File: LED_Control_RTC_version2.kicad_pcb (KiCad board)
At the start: 4 copper layers, 100 x 80 mm, 142 parts, among them J1 Screw_Terminal_01x02, J10 Conn_01x06_Male, J2 Conn_01x02, J3 Conn_02x04_Odd_Even, J4 DS1023-2*8SF11, J5 DS1023-2*8SF11, J6 Conn_01x03_Female, J7 Conn_ARM_JTAG_SWD_10, J8 Conn_ARM_JTAG_SWD_10, J9 Conn_01x06_Male, Q1 IRLR8726TRPBF, Q10 IRLR8726TRPBF, Q11 PJM2309PSA, Q2 IRLR8726TRPBF, Q3 IRLR8726TRPBF, Q4 IRLR8726TRPBF, Q5 IRLR8726TRPBF, Q6 IRLR8726TRPBF, Q7 IRLR8726TRPBF, Q8 IRLR8726TRPBF, Q9 IRLR8726TRPBF, U1 STM32F103C8Tx, U101 TC4427, U102 TC4427, U103 TC4427, U104 TC4427, U105 TC4427, U2 STM32G030C6Tx, U3 AT24C16D-XHM-B, U4 MAX3485, U5 TPS5401, U6 LM1117-3.3, Y1 16MHz, Y2 32.768KHz

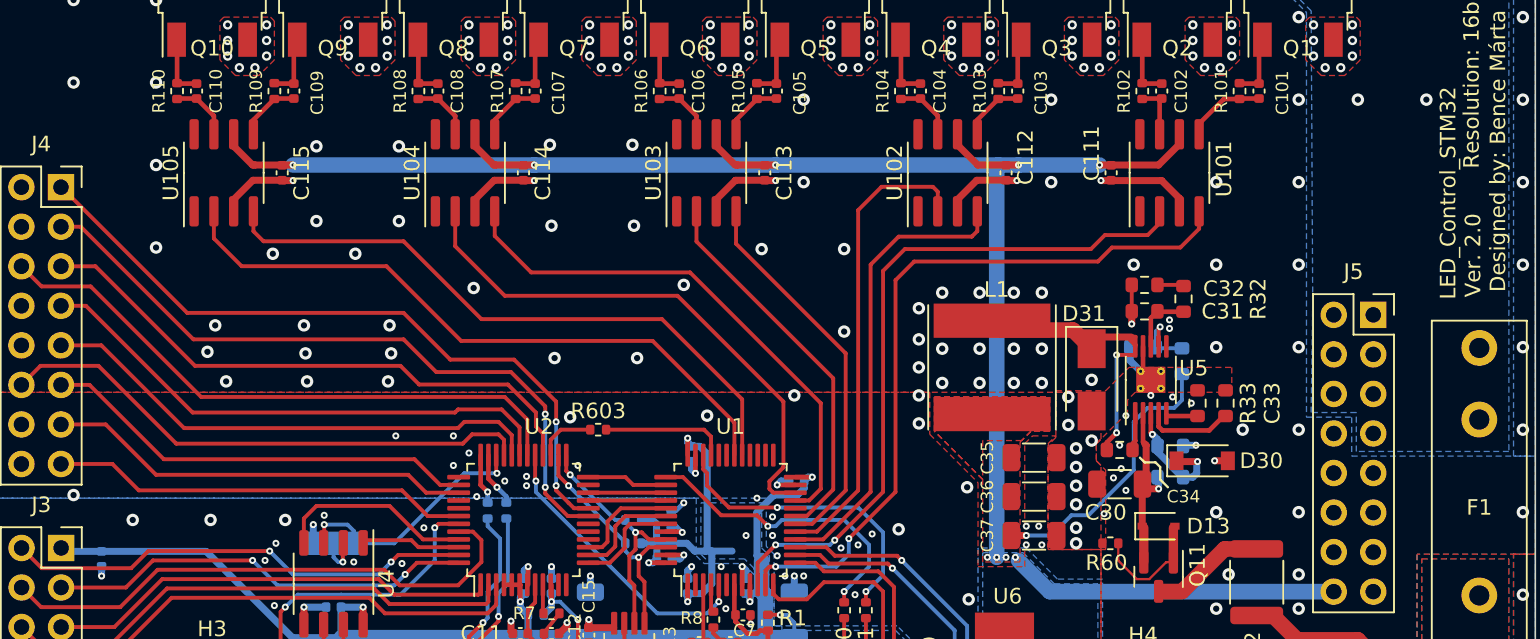
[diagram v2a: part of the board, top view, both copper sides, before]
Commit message: Added more GND vias
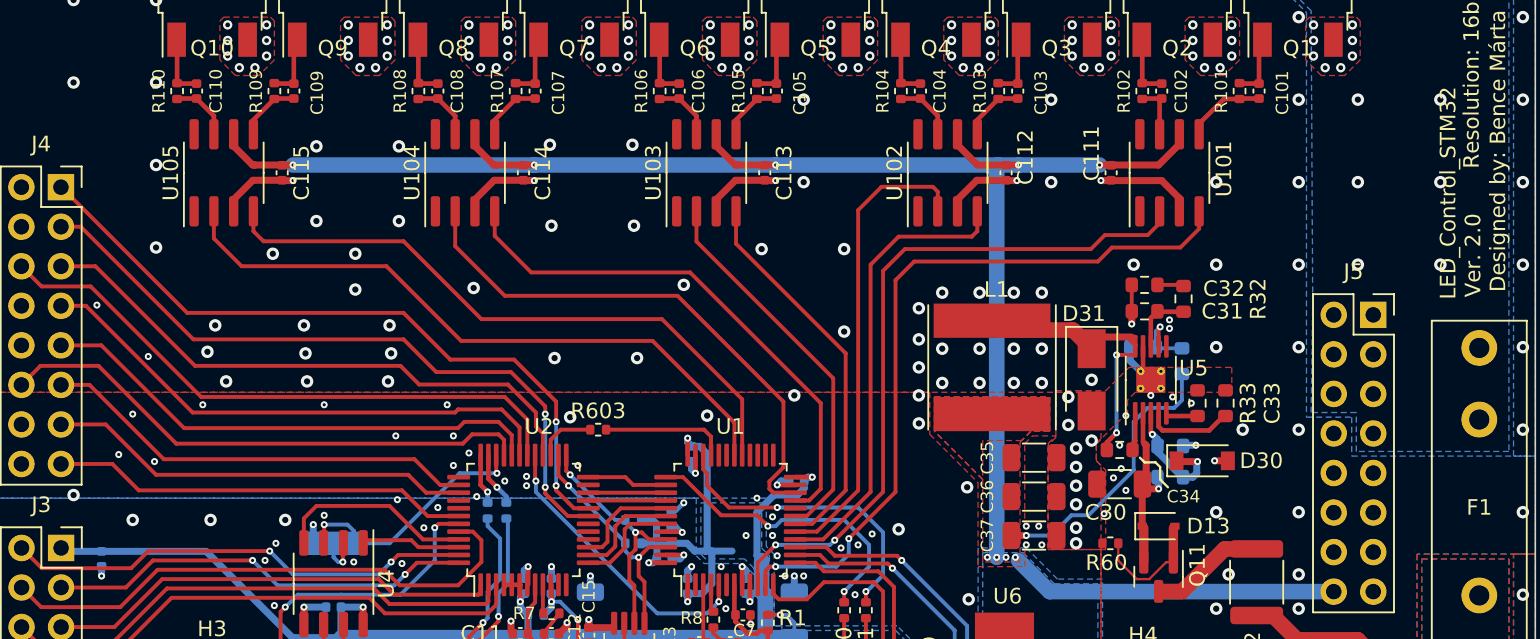
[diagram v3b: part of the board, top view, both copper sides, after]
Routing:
- net GND: vias 369 -> 384
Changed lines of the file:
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@@
   (via (at 165.25 79.5) (size 0.6) (drill 0.3) (layers "F.Cu" "B.Cu") (net 2))
   (via (at 140.3 111.55) (size 0.45) (drill 0.2) (layers "F.Cu" "B.Cu") (free) (net 2))
+  (via (at 125.1 101.9) (size 0.45) (drill 0.2) (layers "F.Cu" "B.Cu") (net 2))
   (via (at 163.3 98.3) (size 0.8) (drill 0.4) (layers "F.Cu" "B.Cu") (free) (net 2))
   (via (at 174.5 92.9) (size 0.8) (drill 0.4) (layers "F.Cu" "B.Cu") (free) (net 2))
@@
   (via (at 159.3 98.3) (size 0.8) (drill 0.4) (layers "F.Cu" "B.Cu") (free) (net 2))
   (via (at 159.25 80.25) (size 0.6) (drill 0.3) (layers "F.Cu" "B.Cu") (net 2))
+  (via (at 188.9 92.9) (size 0.8) (drill 0.4) (layers "F.Cu" "B.Cu") (free) (net 2))
   (via (at 101.1 81.2) (size 0.8) (drill 0.4) (layers "F.Cu" "B.Cu") (free) (net 2))
   (via (at 109.9 109.3) (size 0.8) (drill 0.4) (layers "F.Cu" "B.Cu") (free) (net 2))
@@
   (via (at 127 107.8) (size 0.45) (drill 0.2) (layers "F.Cu" "B.Cu") (net 2))
   (via (at 182.3 119.5) (size 0.8) (drill 0.4) (layers "F.Cu" "B.Cu") (free) (net 2))
+  (via (at 183.6 82.3) (size 0.8) (drill 0.4) (layers "F.Cu" "B.Cu") (free) (net 2))
   (via (at 151.3 114.1) (size 0.45) (drill 0.2) (layers "F.Cu" "B.Cu") (free) (net 2))
   (via (at 129 78.5) (size 0.6) (drill 0.3) (layers "F.Cu" "B.Cu") (net 2))
@@
   (via (at 115.9 96.8) (size 0.8) (drill 0.4) (layers "F.Cu" "B.Cu") (free) (net 2))
   (via (at 95.8 123.6) (size 0.8) (drill 0.4) (layers "F.Cu" "B.Cu") (free) (net 2))
+  (via (at 105.9 98.8) (size 0.45) (drill 0.2) (layers "F.Cu" "B.Cu") (net 2))
   (via (at 119.2 92.2) (size 0.8) (drill 0.4) (layers "F.Cu" "B.Cu") (free) (net 2))
   (via (at 129 79.5) (size 0.6) (drill 0.3) (layers "F.Cu" "B.Cu") (net 2))
@@
   (via (at 142 77.5) (size 0.6) (drill 0.3) (layers "F.Cu" "B.Cu") (net 2))
   (via (at 155.4 99.5) (size 0.8) (drill 0.4) (layers "F.Cu" "B.Cu") (free) (net 2))
+  (via (at 188.9 82.3) (size 0.8) (drill 0.4) (layers "F.Cu" "B.Cu") (free) (net 2))
   (via (at 194.2 103.5) (size 0.8) (drill 0.4) (layers "F.Cu" "B.Cu") (free) (net 2))
   (via (at 135 80.25) (size 0.6) (drill 0.3) (layers "F.Cu" "B.Cu") (net 2))
@@
   (via (at 145.3 91.9) (size 0.8) (drill 0.4) (layers "F.Cu" "B.Cu") (free) (net 2))
   (via (at 161.4 126) (size 0.45) (drill 0.2) (layers "F.Cu" "B.Cu") (free) (net 2))
+  (via (at 119.2 94.5) (size 0.8) (drill 0.4) (layers "F.Cu" "B.Cu") (free) (net 2))
   (via (at 116.5 109.6) (size 0.45) (drill 0.2) (layers "F.Cu" "B.Cu") (net 2))
+  (via (at 188.9 87.6) (size 0.8) (drill 0.4) (layers "F.Cu" "B.Cu") (free) (net 2))
   (via (at 181.5 80.25) (size 0.6) (drill 0.3) (layers "F.Cu" "B.Cu") (net 2))
   (via (at 175.5 77.5) (size 0.6) (drill 0.3) (layers "F.Cu" "B.Cu") (net 2))
@@
   (via (at 111 79.5) (size 0.6) (drill 0.3) (layers "F.Cu" "B.Cu") (net 2))
   (via (at 165.25 77.5) (size 0.6) (drill 0.3) (layers "F.Cu" "B.Cu") (net 2))
+  (via (at 117.2 101.9) (size 0.45) (drill 0.2) (layers "F.Cu" "B.Cu") (net 2))
   (via (at 174.5 87.6) (size 0.8) (drill 0.4) (layers "F.Cu" "B.Cu") (free) (net 2))
   (via (at 144.5 77.5) (size 0.6) (drill 0.3) (layers "F.Cu" "B.Cu") (net 2))
@@
   (via (at 136.75 79.5) (size 0.6) (drill 0.3) (layers "F.Cu" "B.Cu") (net 2))
   (via (at 136 80.25) (size 0.6) (drill 0.3) (layers "F.Cu" "B.Cu") (net 2))
+  (via (at 104.9 102.5) (size 0.45) (drill 0.2) (layers "F.Cu" "B.Cu") (net 2))
   (via (at 121.4 96.8) (size 0.8) (drill 0.4) (layers "F.Cu" "B.Cu") (free) (net 2))
   (via (at 130.2 107.1) (size 0.45) (drill 0.2) (layers "F.Cu" "B.Cu") (free) (net 2))
@@
   (via (at 117 55.8) (size 0.8) (drill 0.4) (layers "F.Cu" "B.Cu") (free) (net 2))
   (via (at 133 120.4) (size 0.45) (drill 0.2) (layers "F.Cu" "B.Cu") (free) (net 2))
+  (via (at 183.6 87.6) (size 0.8) (drill 0.4) (layers "F.Cu" "B.Cu") (free) (net 2))
   (via (at 121.25 78.5) (size 0.6) (drill 0.3) (layers "F.Cu" "B.Cu") (net 2))
   (via (at 145 107.9) (size 0.45) (drill 0.2) (layers "F.Cu" "B.Cu") (free) (net 2))
@@
   (via (at 169.2 92.9) (size 0.8) (drill 0.4) (layers "F.Cu" "B.Cu") (free) (net 2))
   (via (at 156.9 94.7) (size 0.8) (drill 0.4) (layers "F.Cu" "B.Cu") (free) (net 2))
+  (via (at 102.6 95.5) (size 0.45) (drill 0.2) (layers "F.Cu" "B.Cu") (net 2))
   (via (at 95.8 81.2) (size 0.8) (drill 0.4) (layers "F.Cu" "B.Cu") (free) (net 2))
   (via (at 167.3 108.9) (size 0.45) (drill 0.2) (layers "F.Cu" "B.Cu") (net 2))
@@
   (via (at 138.2 123.6) (size 0.8) (drill 0.4) (layers "F.Cu" "B.Cu") (free) (net 2))
   (via (at 183.6 120.4) (size 0.8) (drill 0.4) (layers "F.Cu" "B.Cu") (free) (net 2))
+  (via (at 106.3 105.55) (size 0.45) (drill 0.2) (layers "F.Cu" "B.Cu") (net 2))
   (via (at 148.8 134.2) (size 0.8) (drill 0.4) (layers "F.Cu" "B.Cu") (free) (net 2))
+  (via (at 104 105.1) (size 0.45) (drill 0.2) (layers "F.Cu" "B.Cu") (net 2))
   (via (at 102.9 112.9) (size 0.45) (drill 0.2) (layers "F.Cu" "B.Cu") (net 2))
   (via (at 113.5 78.5) (size 0.6) (drill 0.3) (layers "F.Cu" "B.Cu") (net 2))
@@
   (via (at 133.5 105.8) (size 0.45) (drill 0.2) (layers "F.Cu" "B.Cu") (free) (net 2))
   (via (at 148 82.3) (size 0.8) (drill 0.4) (layers "F.Cu" "B.Cu") (free) (net 2))
+  (via (at 121.9 108) (size 0.45) (drill 0.2) (layers "F.Cu" "B.Cu") (net 2))
   (via (at 161.5 98.3) (size 0.8) (drill 0.4) (layers "F.Cu" "B.Cu") (free) (net 2))
   (via (at 179.8 115) (size 0.8) (drill 0.4) (layers "F.Cu" "B.Cu") (free) (net 2))
@@
   (via (at 183.6 121.8) (size 0.8) (drill 0.4) (layers "F.Cu" "B.Cu") (free) (net 2))
   (via (at 128.25 80.25) (size 0.6) (drill 0.3) (layers "F.Cu" "B.Cu") (net 2))
+  (via (at 183.6 92.9) (size 0.8) (drill 0.4) (layers "F.Cu" "B.Cu") (free) (net 2))
   (via (at 167.75 79.5) (size 0.6) (drill 0.3) (layers "F.Cu" "B.Cu") (net 2))
   (via (at 138.2 55.8) (size 0.8) (drill 0.4) (layers "F.Cu" "B.Cu") (free) (net 2))
@@
   (via (at 164.7 134.2) (size 0.8) (drill 0.4) (layers "F.Cu" "B.Cu") (free) (net 2))
   (via (at 126.5 78.5) (size 0.6) (drill 0.3) (layers "F.Cu" "B.Cu") (net 2))
+  (via (at 109.4 101.9) (size 0.45) (drill 0.2) (layers "F.Cu" "B.Cu") (net 2))
   (via (at 146.5 55.8) (size 0.8) (drill 0.4) (layers "F.Cu" "B.Cu") (free) (net 2))
   (via (at 116.1 100.4) (size 0.8) (drill 0.4) (layers "F.Cu" "B.Cu") (free) (net 2))
@@
   (via (at 115.2 87.5) (size 0.45) (drill 0.2) (layers "F.Cu" "B.Cu") (net 2))
   (via (at 163.3 94.7) (size 0.8) (drill 0.4) (layers "F.Cu" "B.Cu") (free) (net 2))
-  (via (at 188 82.3) (size 0.8) (drill 0.4) (layers "F.Cu" "B.Cu") (free) (net 2))
   (via (at 163.1 109.7) (size 0.45) (drill 0.2) (layers "F.Cu" "B.Cu") (net 2))
   (via (at 122.197833 112.1) (size 0.45) (drill 0.2) (layers "F.Cu" "B.Cu") (net 2))
@@
   (via (at 121.3 100.4) (size 0.8) (drill 0.4) (layers "F.Cu" "B.Cu") (free) (net 2))
   (via (at 127.25 80.25) (size 0.6) (drill 0.3) (layers "F.Cu" "B.Cu") (net 2))
+  (via (at 124.5 108.5) (size 0.45) (drill 0.2) (layers "F.Cu" "B.Cu") (net 2))
   (via (at 183.25 79.5) (size 0.6) (drill 0.3) (layers "F.Cu" "B.Cu") (net 2))
   (via (at 118.75 77.5) (size 0.6) (drill 0.3) (layers "F.Cu" "B.Cu") (net 2))
@@
   (via (at 194.2 134.2) (size 0.8) (drill 0.4) (layers "F.Cu" "B.Cu") (free) (net 2))
   (via (at 117.8 119.4) (size 0.45) (drill 0.2) (layers "F.Cu" "B.Cu") (net 2))
-  (via (at 183.6 82.3) (size 0.8) (drill 0.4) (layers "F.Cu" "B.Cu") (free) (net 2))
   (via (at 174.5 115) (size 0.8) (drill 0.4) (layers "F.Cu" "B.Cu") (free) (net 2))
   (via (at 132.4 125.9) (size 0.45) (drill 0.2) (layers "F.Cu" "B.Cu") (free) (net 2))
@@
   (via (at 128.3 106.3) (size 0.45) (drill 0.2) (layers "F.Cu" "B.Cu") (net 98))
   (via (at 117.2 109.6) (size 0.45) (drill 0.2) (layers "F.Cu" "B.Cu") (net 98))
-  (segment (start 128.3 106.3) (end 126.2 106.3) (width 0.25) (layer "B.Cu") (net 98))
+  (segment (start 128.3 106.3) (end 125.9 106.3) (width 0.25) (layer "B.Cu") (net 98))
+  (segment (start 121.4 110.8) (end 119.1 110.8) (width 0.25) (layer "B.Cu") (net 98))
+  (segment (start 125.9 106.3) (end 121.4 110.8) (width 0.25) (layer "B.Cu") (net 98))
   (segment (start 118.7 109.6) (end 117.2 109.6) (width 0.25) (layer "B.Cu") (net 98))
-  (segment (start 126.2 106.3) (end 121.7 110.8) (width 0.25) (layer "B.Cu") (net 98))
   (segment (start 119.1 110.8) (end 119.1 110) (width 0.25) (layer "B.Cu") (net 98))
   (segment (start 119.1 110) (end 118.7 109.6) (width 0.25) (layer "B.Cu") (net 98))
-  (segment (start 121.7 110.8) (end 119.1 110.8) (width 0.25) (layer "B.Cu") (net 98))
   (segment (start 128.3 107.2) (end 127.75 106.65) (width 0.3) (layer "F.Cu") (net 99))
   (segment (start 127.75 106.65) (end 127.75 105.1375) (width 0.3) (layer "F.Cu") (net 99))

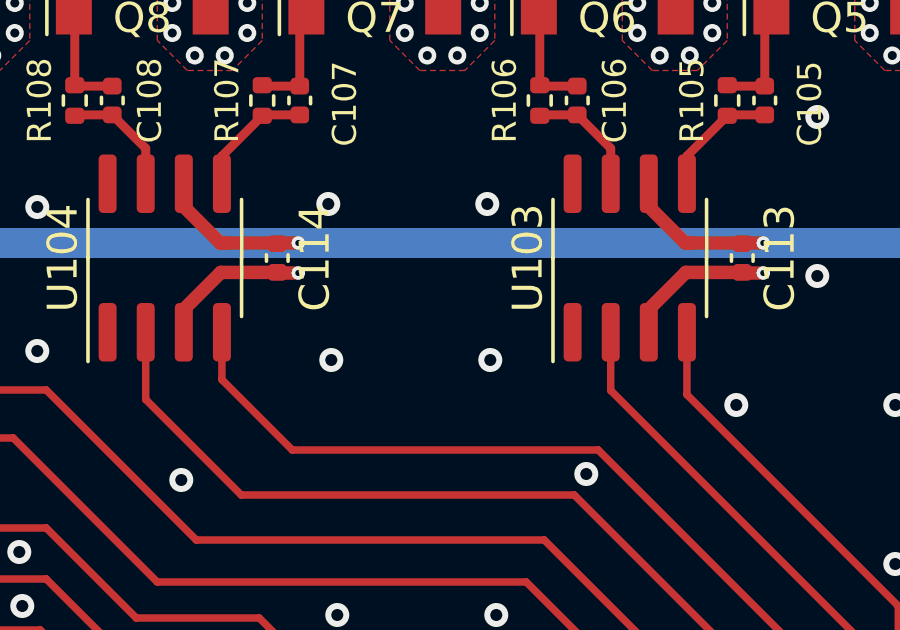
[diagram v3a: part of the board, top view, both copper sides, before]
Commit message: Added FET driver cap
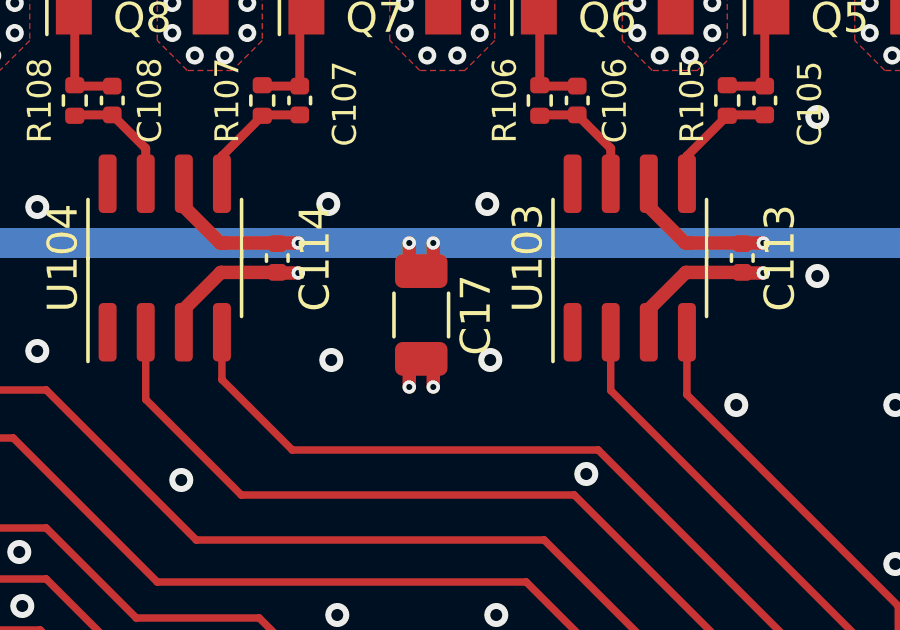
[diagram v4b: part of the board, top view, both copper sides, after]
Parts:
- added C17: 10u, Resistor_SMD:R_1206_3216Metric, F.Cu at (134.8, 88.9)
- renumbered C501 to C18
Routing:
- net GND: track 71.4 -> 73.6 mm, vias 384 -> 386
- net +5V: track 148.5 -> 150.7 mm, vias 18 -> 20
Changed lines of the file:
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@@
     )
   )
+  (footprint "Resistor_SMD:R_1206_3216Metric" (layer "F.Cu")
+    (at 134.8 88.9 -90)
+    (descr "Resistor SMD 1206 (3216 Metric), square (rectangular) end terminal, IPC_7351 nominal, (Body size source: IPC-SM-782 page 72, https://www.pcb-3d.com/wordpress/wp-content/uploads/ipc-sm-782a_amendment_1_and_2.pdf), generated with kicad-footprint-generator")
+    (tags "resistor")
+    (property "Sheetfile" "MCU_Peripherals.kicad_sch")
+    (property "Sheetname" "MCUs + Peripherals")
+    (attr smd)
+    (fp_text reference "C17" (at 0 -1.82 90) (layer "F.SilkS")
+      (effects (font (size 1 1) (thickness 0.15)))
+    )
+    (fp_text value "10u" (at 0 1.82 90) (layer "F.Fab")
+      (effects (font (size 1 1) (thickness 0.15)))
+    )
+    (fp_text user "${REFERENCE}" (at 0 0 90) (layer "F.Fab")
+      (effects (font (size 0.8 0.8) (thickness 0.12)))
+    )
+    (fp_line (start -0.727064 0.91) (end 0.727064 0.91) (layer "F.SilkS") (width 0.12))
+    (fp_line (start -0.727064 -0.91) (end 0.727064 -0.91) (layer "F.SilkS") (width 0.12))
+    (fp_line (start 2.28 -1.12) (end 2.28 1.12) (layer "F.CrtYd") (width 0.05))
+    (fp_line (start 2.28 1.12) (end -2.28 1.12) (layer "F.CrtYd") (width 0.05))
+    (fp_line (start -2.28 1.12) (end -2.28 -1.12) (layer "F.CrtYd") (width 0.05))
+    (fp_line (start -2.28 -1.12) (end 2.28 -1.12) (layer "F.CrtYd") (width 0.05))
+    (fp_line (start 1.6 0.8) (end -1.6 0.8) (layer "F.Fab") (width 0.1))
+    (fp_line (start 1.6 -0.8) (end 1.6 0.8) (layer "F.Fab") (width 0.1))
+    (fp_line (start -1.6 0.8) (end -1.6 -0.8) (layer "F.Fab") (width 0.1))
+    (fp_line (start -1.6 -0.8) (end 1.6 -0.8) (layer "F.Fab") (width 0.1))
+    (pad "1" smd roundrect (at -1.4625 0 270) (size 1.125 1.75) (layers "F.Cu" "F.Paste" "F.Mask") (roundrect_rratio 0.222222)
+      (net 29 "+5V") (pintype "passive"))
+    (pad "2" smd roundrect (at 1.4625 0 270) (size 1.125 1.75) (layers "F.Cu" "F.Paste" "F.Mask") (roundrect_rratio 0.222222)
+      (net 2 "GND") (pintype "passive"))
+    (model "${KICAD6_3DMODEL_DIR}/Resistor_SMD.3dshapes/R_1206_3216Metric.wrl"
+      (offset (xyz 0 0 0))
+      (scale (xyz 1 1 1))
+      (rotate (xyz 0 0 0))
+    )
+  )
   (footprint "Capacitor_SMD:C_0402_1005Metric" (layer "F.Cu")
     (at 155.5 81.75 90)
@@
     (property "Sheetname" "MCUs + Peripherals")
     (attr smd)
-    (fp_text reference "C501" (at 0 1.16 90) (layer "B.SilkS")
+    (fp_text reference "C18" (at 0 1.16 90) (layer "B.SilkS")
       (effects (font (size 1 1) (thickness 0.15)) (justify mirror))
     )
@@
   (segment (start 141.32 104.57) (end 141.8 105.05) (width 0.45) (layer "B.Cu") (net 1))
   (segment (start 158.6 124) (end 158.6 122.55) (width 0.45) (layer "F.Cu") (net 2))
+  (segment (start 134.4 90.7625) (end 134.8 90.3625) (width 0.45) (layer "F.Cu") (net 2))
   (segment (start 144.05 113.4625) (end 144.05 112.3) (width 0.3) (layer "F.Cu") (net 2))
   (segment (start 141.05 105.1375) (end 141.05 106.3) (width 0.3) (layer "F.Cu") (net 2))
@@
   (segment (start 111.385 88.715) (end 112.62 87.48) (width 0.45) (layer "F.Cu") (net 2))
   (segment (start 161.7 87.5) (end 161.02 87.5) (width 0.45) (layer "F.Cu") (net 2))
+  (segment (start 135.2 91.3) (end 135.2 90.7625) (width 0.45) (layer "F.Cu") (net 2))
   (segment (start 167 133.2) (end 168.3 133.2) (width 0.45) (layer "F.Cu") (net 2))
   (segment (start 144.3 117.8) (end 143.76 117.26) (width 0.45) (layer "F.Cu") (net 2))
@@
   (segment (start 169.8 98.15) (end 169.8 99.6) (width 0.3) (layer "F.Cu") (net 2))
   (segment (start 132.8 116.1) (end 132.3 116.6) (width 0.45) (layer "F.Cu") (net 2))
+  (segment (start 135.2 90.7625) (end 134.8 90.3625) (width 0.45) (layer "F.Cu") (net 2))
   (segment (start 142.385 88.715) (end 143.62 87.48) (width 0.45) (layer "F.Cu") (net 2))
   (segment (start 132.8 115.9) (end 132.8 116.1) (width 0.45) (layer "F.Cu") (net 2))
@@
   (segment (start 142.385 89.475) (end 142.385 88.715) (width 0.45) (layer "F.Cu") (net 2))
   (segment (start 129.2 115.8) (end 129.2 116.48) (width 0.45) (layer "F.Cu") (net 2))
+  (segment (start 134.4 91.3) (end 134.4 90.7625) (width 0.45) (layer "F.Cu") (net 2))
   (segment (start 129.2 116.48) (end 129.32 116.6) (width 0.45) (layer "F.Cu") (net 2))
   (segment (start 169.075 96.705671) (end 169.075 95.9) (width 0.45) (layer "F.Cu") (net 2))
@@
   (via (at 179.8 82.3) (size 0.8) (drill 0.4) (layers "F.Cu" "B.Cu") (free) (net 2))
   (via (at 180.75 79.5) (size 0.6) (drill 0.3) (layers "F.Cu" "B.Cu") (net 2))
+  (via (at 134.4 91.3) (size 0.45) (drill 0.2) (layers "F.Cu" "B.Cu") (net 2))
   (via (at 131.7 85.2) (size 0.8) (drill 0.4) (layers "F.Cu" "B.Cu") (free) (net 2))
   (via (at 166.5 100.3) (size 0.8) (drill 0.4) (layers "F.Cu" "B.Cu") (free) (net 2))
@@
   (via (at 115.2 87.5) (size 0.45) (drill 0.2) (layers "F.Cu" "B.Cu") (net 2))
   (via (at 163.3 94.7) (size 0.8) (drill 0.4) (layers "F.Cu" "B.Cu") (free) (net 2))
+  (via (at 135.2 91.3) (size 0.45) (drill 0.2) (layers "F.Cu" "B.Cu") (net 2))
   (via (at 163.1 109.7) (size 0.45) (drill 0.2) (layers "F.Cu" "B.Cu") (net 2))
   (via (at 122.197833 112.1) (size 0.45) (drill 0.2) (layers "F.Cu" "B.Cu") (net 2))
@@
   (segment (start 163.175 122.575) (end 163.2 122.55) (width 0.45) (layer "F.Cu") (net 29))
   (segment (start 159.175 86.5) (end 157.885 85.21) (width 0.45) (layer "F.Cu") (net 29))
+  (segment (start 134.4 86.5) (end 134.4 87.0375) (width 0.45) (layer "F.Cu") (net 29))
   (segment (start 112.77 86.5) (end 112.6 86.5) (width 0.45) (layer "F.Cu") (net 29))
   (segment (start 126.885 85.285) (end 126.885 84.505) (width 0.45) (layer "F.Cu") (net 29))
@@
   (segment (start 172.115 85.185) (end 172.115 84.545) (width 0.45) (layer "F.Cu") (net 29))
   (segment (start 163.2 122.55) (end 166.25 122.55) (width 1) (layer "F.Cu") (net 29))
+  (segment (start 135.2 87.0375) (end 134.8 87.4375) (width 0.45) (layer "F.Cu") (net 29))
+  (segment (start 135.2 86.5) (end 135.2 87.0375) (width 0.45) (layer "F.Cu") (net 29))
+  (segment (start 134.4 87.0375) (end 134.8 87.4375) (width 0.45) (layer "F.Cu") (net 29))
   (segment (start 143.6 86.5) (end 142.385 85.285) (width 0.45) (layer "F.Cu") (net 29))
   (segment (start 143.77 86.5) (end 143.6 86.5) (width 0.45) (layer "F.Cu") (net 29))
@@
   (via (at 164.95 124.65) (size 0.45) (drill 0.2) (layers "F.Cu" "B.Cu") (free) (net 29))
   (via (at 161.6 111.7) (size 0.45) (drill 0.2) (layers "F.Cu" "B.Cu") (free) (net 29))
+  (via (at 134.4 86.5) (size 0.45) (drill 0.2) (layers "F.Cu" "B.Cu") (net 29))
   (via (at 130.7 86.5) (size 0.45) (drill 0.2) (layers "F.Cu" "B.Cu") (net 29))
   (via (at 165.5 125.2) (size 0.45) (drill 0.2) (layers "F.Cu" "B.Cu") (free) (net 29))
@@
   (via (at 146.2 86.5) (size 0.45) (drill 0.2) (layers "F.Cu" "B.Cu") (net 29))
   (via (at 162.3 110.3) (size 0.45) (drill 0.2) (layers "F.Cu" "B.Cu") (net 29))
+  (via (at 135.2 86.5) (size 0.45) (drill 0.2) (layers "F.Cu" "B.Cu") (net 29))
   (via (at 160.4 111.7) (size 0.45) (drill 0.2) (layers "F.Cu" "B.Cu") (free) (net 29))
   (via (at 164.95 123.55) (size 0.45) (drill 0.2) (layers "F.Cu" "B.Cu") (free) (net 29))
